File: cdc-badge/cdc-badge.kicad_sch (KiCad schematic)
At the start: 157 parts, among them J1 USB_C, J2 JST S2B-PH-SM4-TB, J3 Conn_02x20_Odd_Even, J4 Conn_Grove, J5 Conn_02x03_Odd_Even, J6 Conn_01x06, J7 Conn_01x24, Q1 Si1308EDL, Q2 Si1308EDL, SW0 0, SW1 1, SW10 YES, SW11 NO, SW12 power on/reset, SW13 reset, SW14 flash/power off, SW15 MST-22D18G2 3J, SW16 MST-22D18G2 3J, SW2 2, SW3 3, SW4 4, SW5 5, SW6 6, SW7 7, SW8 8, SW9 9, U1 ESP32-S3-WROOM-1-N16R8, U2 TCA9535PWR, U3 TR01-C2P-T301, U5 TLV61070ADBVR, U6 BQ25895RTW, U8 TLV62569DBV

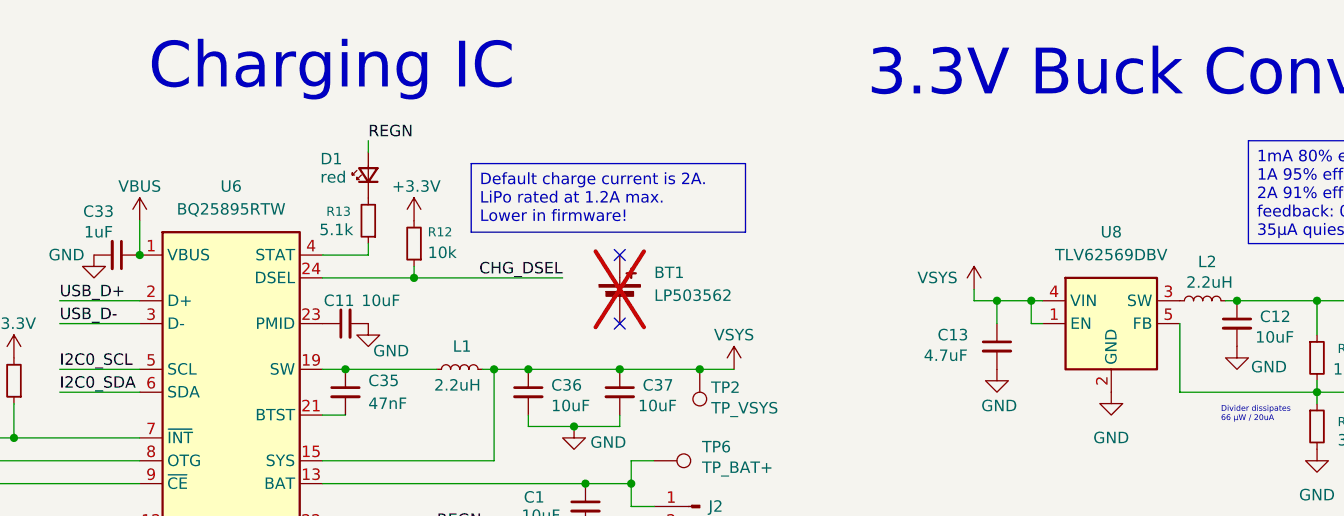
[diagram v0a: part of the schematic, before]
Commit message: Add MPN to all symbols.
Makes BOM ready for other manufacturers besides JLCPCB.
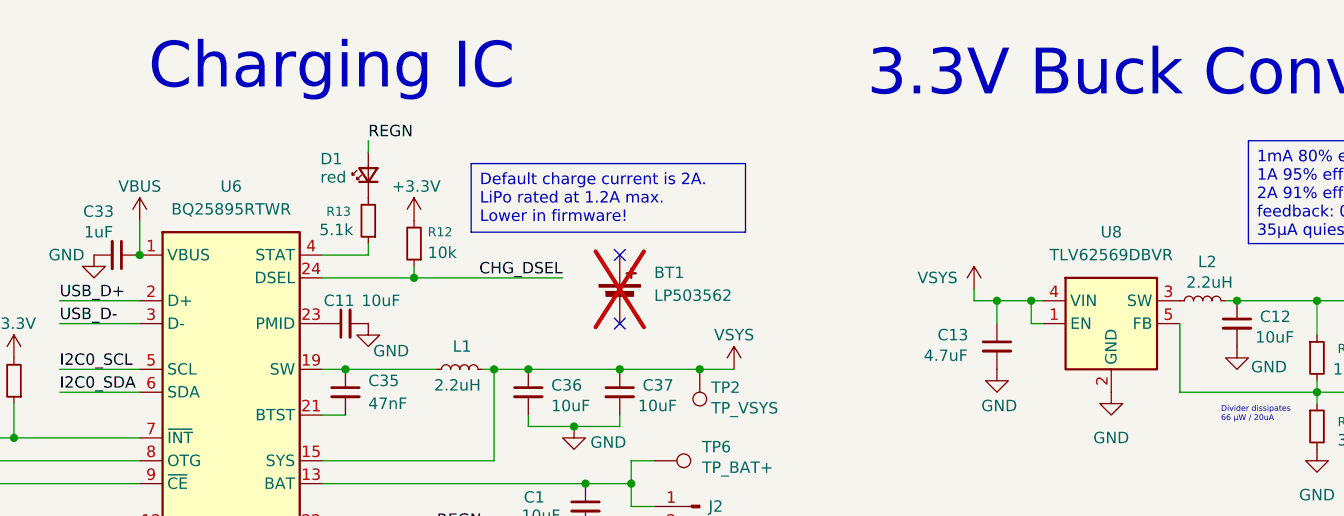
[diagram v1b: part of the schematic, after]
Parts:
- C1, C11, C12, C36, C37, C5, C6, C7, C8, C9: MPN (none) -> CL21A106KAYNNNE
- C10, C15, C16, C17, C18, C19, C2, C20, C21, C22, C25, C26, C27, C28, C29, C3, C30, C31, C32, C4: MPN (none) -> CC0603KRX7R9BB104
- C33: MPN (none) -> CL10A105KB8NNNC
- C35: MPN (none) -> CL10B473KB8NNNC
- D3: MPN (none) -> SMF14CA
- D7, D8: MPN (none) -> H3V3U06B
- J1: MPN (none) -> TYPE-C 16PIN 2MD(073)
- Q1, Q2: MPN (none) -> SI1308EDL
- R10, R16, R18, R23, R24, R25, R26, R27, R28, R29, R3, R30, R31, R36, R37, R38, R39, R40: MPN (none) -> 0603WAF4702T5E
- R12, R14, R15, R20, R4, R42, R43, R46, R47, R5, R6, R8, R9: MPN (none) -> 0603WAF1002T5E
- R32: MPN (none) -> 0603WAF510KT5E
- SW15, SW16: MPN (none) -> MST-22D18G2 3J
- U1: MPN (none) -> ESP32-S3-WROOM-1-N16R8
- U2: MPN (none) -> TCA9535PWR
- U5: MPN (none) -> TLV61070ADBVR
- U6: value BQ25895RTW -> BQ25895RTWR; MPN (none) -> BQ25895RTWR
- U8: value TLV62569DBV -> TLV62569DBVR; MPN (none) -> TLV62569DBVR

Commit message: setup exports, remove unpopulated from BOM
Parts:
- R36, R42, R43, TP1, TP2, TP6, TP7: now left out of the parts list
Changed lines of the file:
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@@
 		(unit 1)
 		(exclude_from_sim no)
-		(in_bom yes)
+		(in_bom no)
 		(on_board yes)
 		(dnp no)
@@
 		(unit 1)
 		(exclude_from_sim no)
-		(in_bom yes)
+		(in_bom no)
 		(on_board yes)
 		(dnp no)
@@
 		(unit 1)
 		(exclude_from_sim no)
-		(in_bom yes)
+		(in_bom no)
 		(on_board yes)
 		(dnp no)
@@
 		(unit 1)
 		(exclude_from_sim no)
-		(in_bom yes)
+		(in_bom no)
 		(on_board yes)
 		(dnp yes)
@@
 		(unit 1)
 		(exclude_from_sim no)
-		(in_bom yes)
+		(in_bom no)
 		(on_board yes)
 		(dnp yes)
@@
 		(unit 1)
 		(exclude_from_sim no)
-		(in_bom yes)
+		(in_bom no)
 		(on_board yes)
 		(dnp yes)
@@
 		(unit 1)
 		(exclude_from_sim no)
-		(in_bom yes)
+		(in_bom no)
 		(on_board yes)
 		(dnp no)

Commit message: Enlarge vias in ESP32 and BQ25895 FPs from 0.2 to 0.3 mm
Makes production cheaper.
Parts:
- U6: footprint Package_DFN_QFN:Texas_RTW_WQFN-24-1EP_4x4mm_P0.5mm_EP2.7x2.7mm_ThermalVias -> CDC_Badge:Texas_RTW_WQFN-24-1EP_4x4mm_P0.5mm_EP2.7x2.7mm_0.3mmThermalVias
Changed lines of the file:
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@@
 			)
 		)
-		(property "Footprint" "Package_DFN_QFN:Texas_RTW_WQFN-24-1EP_4x4mm_P0.5mm_EP2.7x2.7mm_ThermalVias"
+		(property "Footprint" "CDC_Badge:Texas_RTW_WQFN-24-1EP_4x4mm_P0.5mm_EP2.7x2.7mm_0.3mmThermalVias"
 			(at 143.51 92.964 0)
 			(effects

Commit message: Grove connector: new MPN to work with NextPCB
Fix datasheet links in BOOMELE footprints.
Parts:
- J4: MPN HY-4P (A2006WF-04A) -> HC-HY-4AWT
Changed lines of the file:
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@@
 			)
 		)
-		(property "MPN" "HY-4P (A2006WF-04A)"
+		(property "MPN" "HC-HY-4AWT"
 			(at 254 205.74 0)
 			(effects

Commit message: schematic: fix, battery connector was not in BOM
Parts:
- J2: now in the parts list
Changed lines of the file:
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@@
 		(unit 1)
 		(exclude_from_sim no)
-		(in_bom no)
+		(in_bom yes)
 		(on_board yes)
 		(dnp no)

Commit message: pcb: test points, vias, islands
Test points are now SMD again for better aesthetics.
Review via placement.
Fix islands.
Fix silkscreen to via overlap.
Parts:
- TP1, TP2, TP6, TP7: footprint TestPoint:TestPoint_THTPad_D2.0mm_Drill1.0mm -> TestPoint:TestPoint_Pad_D2.0mm
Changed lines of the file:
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@@
 			)
 		)
-		(property "Footprint" "TestPoint:TestPoint_THTPad_D2.0mm_Drill1.0mm"
+		(property "Footprint" "TestPoint:TestPoint_Pad_D2.0mm"
 			(at 190.5 58.42 0)
 			(effects
@@
 			)
 		)
-		(property "Footprint" "TestPoint:TestPoint_THTPad_D2.0mm_Drill1.0mm"
+		(property "Footprint" "TestPoint:TestPoint_Pad_D2.0mm"
 			(at 69.85 44.45 0)
 			(effects
@@
 			)
 		)
-		(property "Footprint" "TestPoint:TestPoint_THTPad_D2.0mm_Drill1.0mm"
+		(property "Footprint" "TestPoint:TestPoint_Pad_D2.0mm"
 			(at 190.5 73.66 0)
 			(effects
@@
 			)
 		)
-		(property "Footprint" "TestPoint:TestPoint_THTPad_D2.0mm_Drill1.0mm"
+		(property "Footprint" "TestPoint:TestPoint_Pad_D2.0mm"
 			(at 193.04 86.36 0)
 			(effects

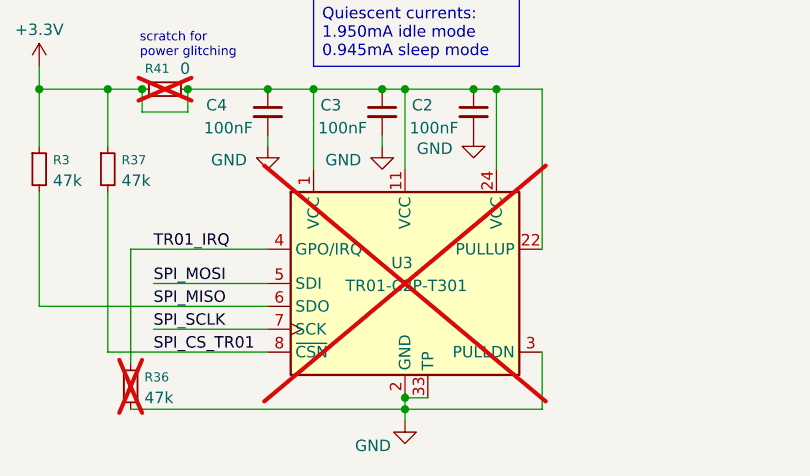
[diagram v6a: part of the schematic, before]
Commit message: schematic: populate TROPIC01
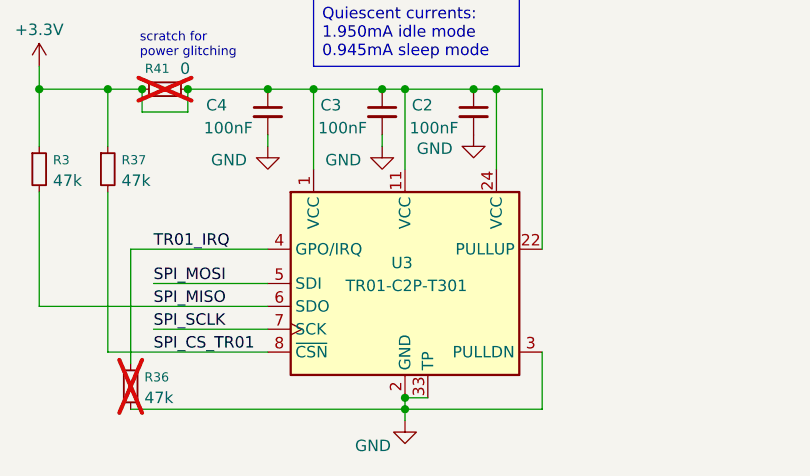
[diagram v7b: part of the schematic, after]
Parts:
- U3: JLCPCB PN (none) -> C9900235223; now fitted; now in the parts list
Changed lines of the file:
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@@
 		(unit 1)
 		(exclude_from_sim no)
-		(in_bom no)
+		(in_bom yes)
 		(on_board yes)
-		(dnp yes)
+		(dnp no)
 		(property "Reference" "U3"
 			(at 275.336 261.874 0)
@@
 			(effects
 				(font
+					(size 1.27 1.27)
+				)
+				(hide yes)
+			)
+		)
+		(property "JLCPCB PN" "C9900235223"
+			(at 276.86 264.16 0)
+			(effects
+				(font

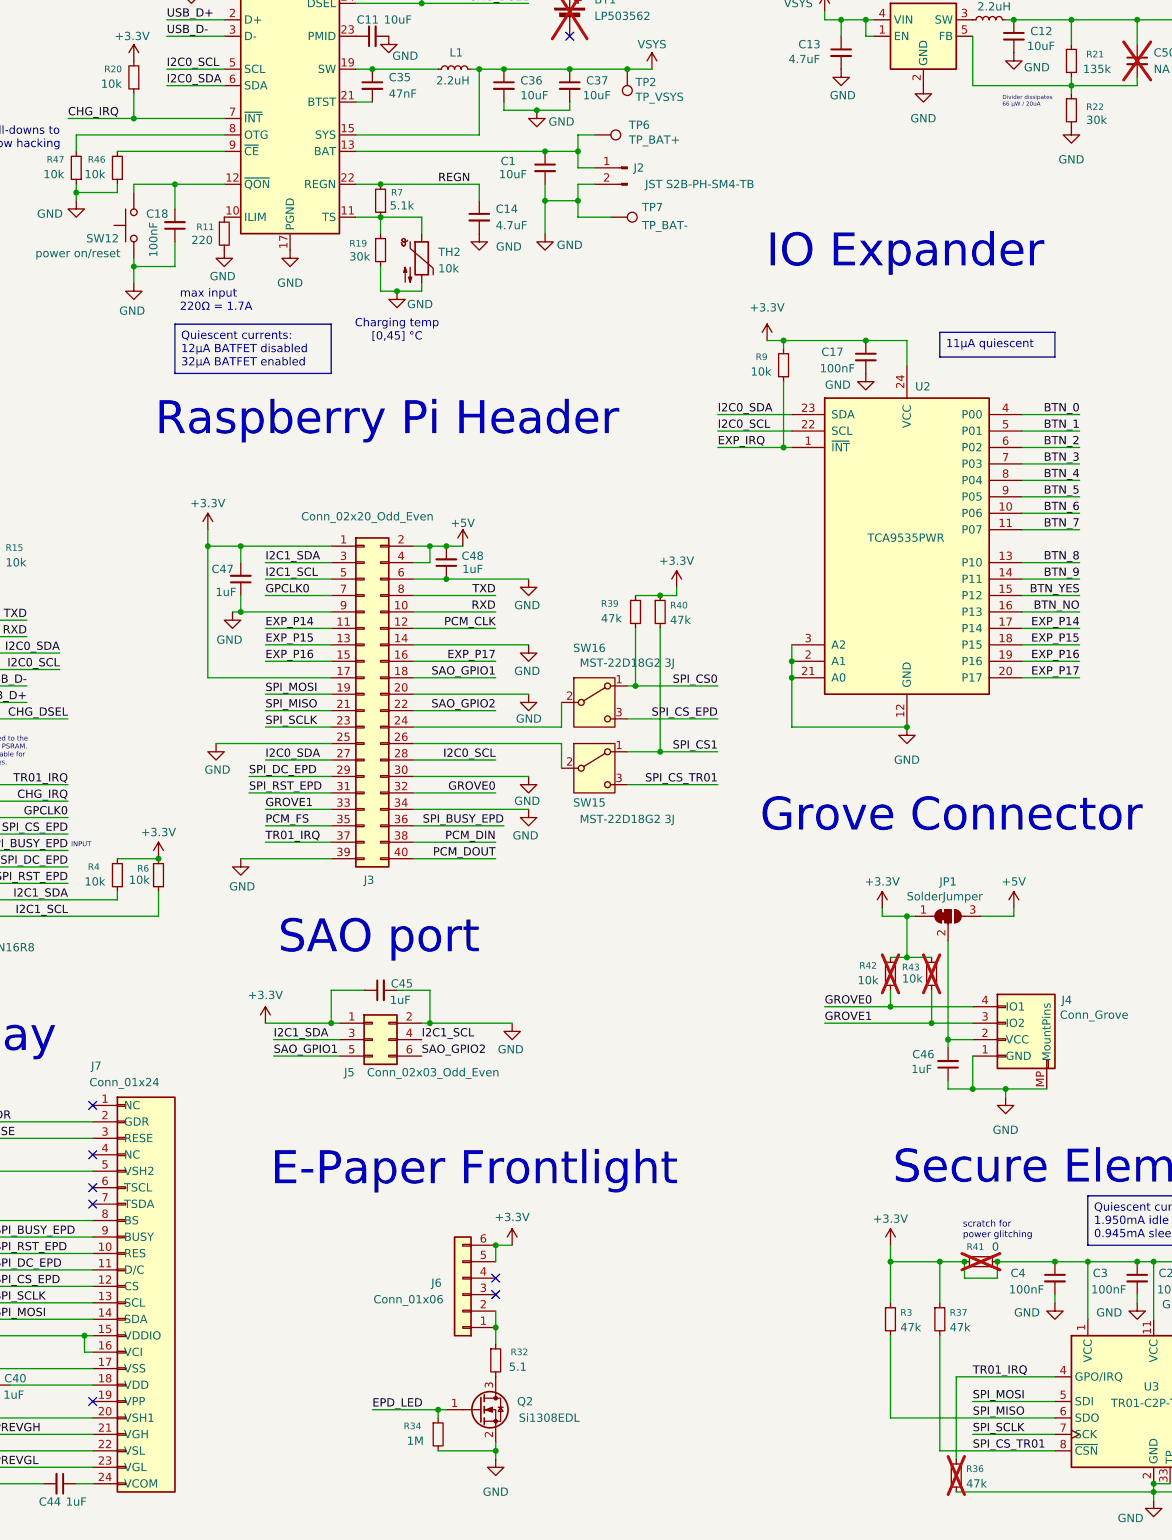
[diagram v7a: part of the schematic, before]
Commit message: schematic: add mounting pins to battery connector
Fixes liking with PCB.
Remove non-generic fields from symbols.
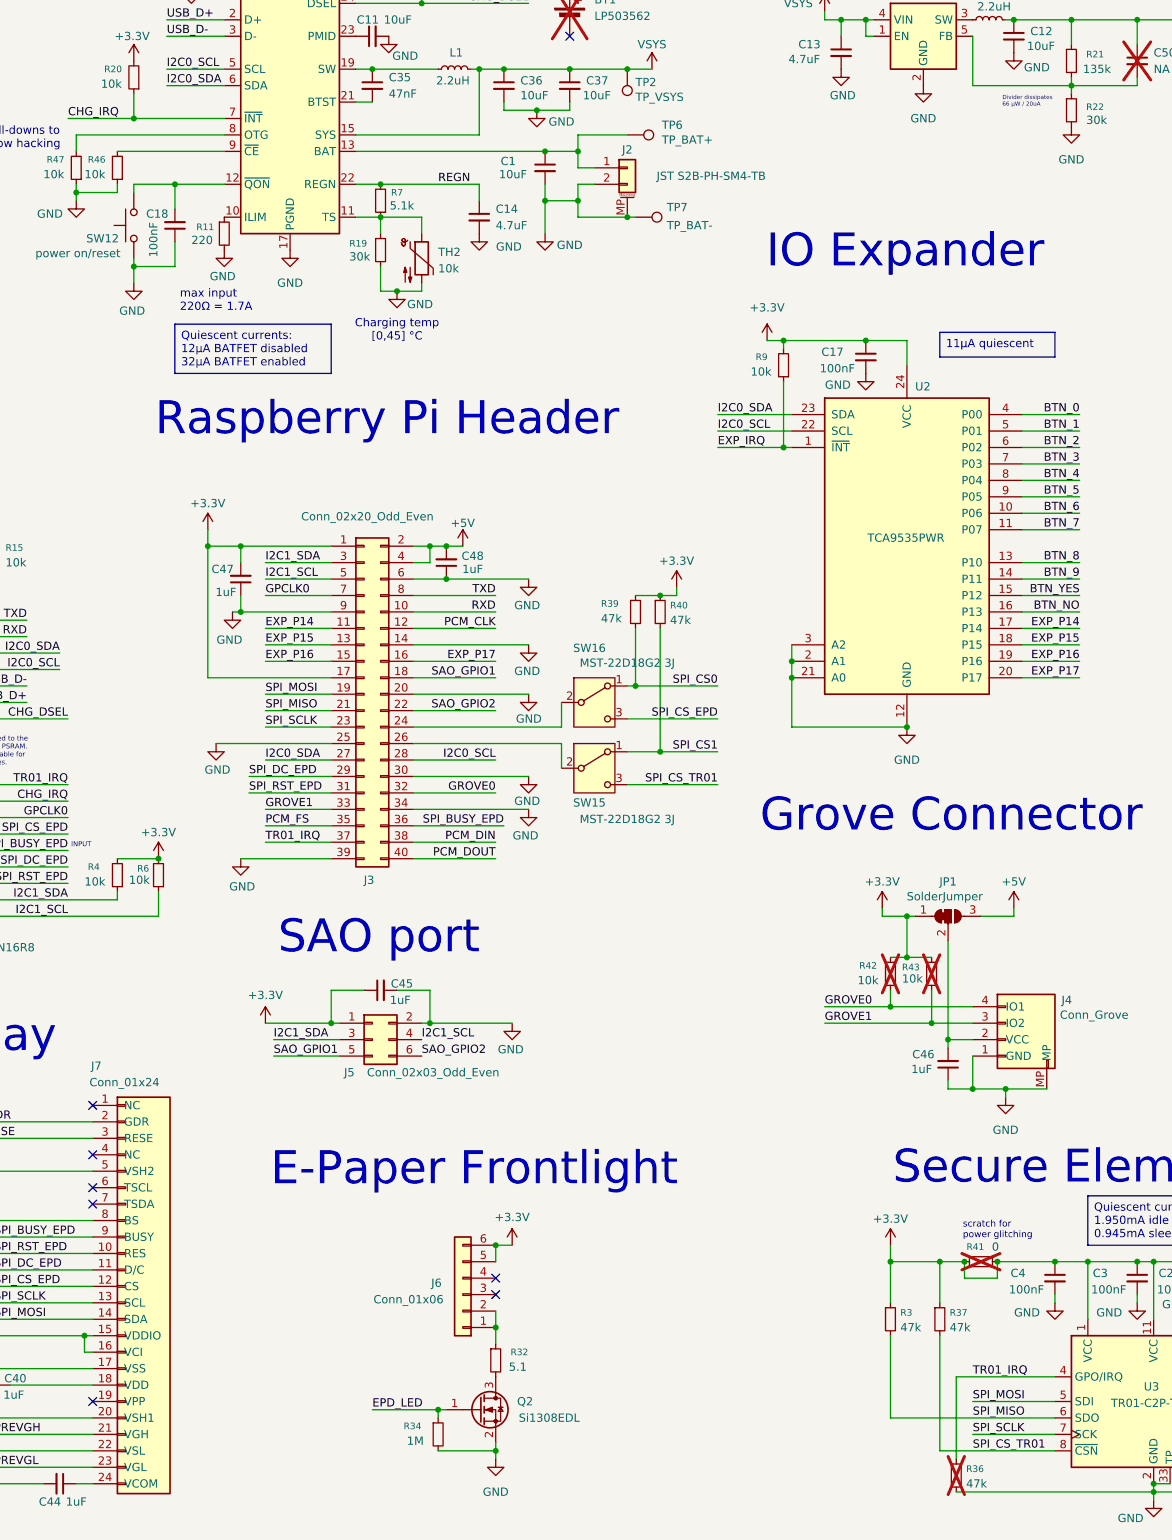
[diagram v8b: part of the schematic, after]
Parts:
- J2: symbol Connector:Conn_01x02_Pin -> Connector_Generic_MountingPin:Conn_01x02_MountingPin
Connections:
- net GND: now also J2.MP (MountPin)
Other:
- moved on the sheet: J4, TP6, TP7
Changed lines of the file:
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@@
 	)
 	(junction
+		(at 195.58 81.28)
+		(diameter 0)
+		(color 0 0 0 0)
+	)
+	(junction
 		(at 243.84 242.57)
 		(diameter 0)
@@
 	(wire
 		(pts
+			(xy 196.85 81.28) (xy 195.58 81.28)
+		)
+		(stroke
+			(width 0)
+			(type default)
+		)
+	)
+	(wire
+		(pts
 			(xy 92.71 229.87) (xy 92.71 228.6)
 		)
@@
 	(wire
 		(pts
-			(xy 193.04 81.28) (xy 187.96 81.28)
+			(xy 195.58 81.28) (xy 187.96 81.28)
 		)
 		(stroke
@@
 	(wire
 		(pts
-			(xy 190.5 68.58) (xy 187.96 68.58)
+			(xy 195.58 68.58) (xy 187.96 68.58)
 		)
 		(stroke
@@
 	(symbol
 		(lib_id "Connector:TestPoint")
-		(at 190.5 68.58 270)
+		(at 195.58 68.58 270)
 		(unit 1)
 		(exclude_from_sim no)
@@
 		(dnp no)
 		(property "Reference" "TP6"
-			(at 195.834 67.056 90)
+			(at 200.914 67.056 90)
 			(effects
 				(font
@@
 		)
 		(property "Value" "TP_BAT+"
-			(at 195.834 69.342 90)
+			(at 200.914 69.342 90)
 			(effects
 				(font
@@
 		)
 		(property "Footprint" "TestPoint:TestPoint_Pad_D2.0mm"
-			(at 190.5 73.66 0)
+			(at 195.58 73.66 0)
 			(effects
 				(font
@@
 		)
 		(property "Datasheet" "~"
-			(at 190.5 73.66 0)
+			(at 195.58 73.66 0)
 			(effects
 				(font
@@
 		)
 		(property "Description" "test point"
-			(at 190.5 68.58 0)
+			(at 195.58 68.58 0)
 			(effects
 				(font
@@
 	(symbol
 		(lib_id "Connector:TestPoint")
-		(at 193.04 81.28 270)
+		(at 196.85 81.28 270)
 		(unit 1)
 		(exclude_from_sim no)
@@
 		(dnp no)
 		(property "Reference" "TP7"
-			(at 197.866 79.756 90)
+			(at 201.676 79.756 90)
 			(effects
 				(font
@@
 		)
 		(property "Value" "TP_BAT-"
-			(at 197.866 82.55 90)
+			(at 201.676 82.55 90)
 			(effects
 				(font
@@
 		)
 		(property "Footprint" "TestPoint:TestPoint_Pad_D2.0mm"
-			(at 193.04 86.36 0)
+			(at 196.85 86.36 0)
 			(effects
 				(font
@@
 		)
 		(property "Datasheet" "~"
-			(at 193.04 86.36 0)
+			(at 196.85 86.36 0)
 			(effects
 				(font
@@
 		)
 		(property "Description" "test point"
-			(at 193.04 81.28 0)
+			(at 196.85 81.28 0)
 			(effects
 				(font
@@
 	)
 	(symbol
-		(lib_id "Connector:Conn_01x02_Pin")
+		(lib_id "Connector_Generic_MountingPin:Conn_01x02_MountingPin")
 		(at 195.58 73.66 0)
-		(mirror y)
 		(unit 1)
 		(exclude_from_sim no)
@@
 		(dnp no)
 		(property "Reference" "J2"
-			(at 197.358 73.66 0)
+			(at 195.58 70.866 0)
 			(effects
 				(font
@@
 		)
 		(property "Value" "JST S2B-PH-SM4-TB"
-			(at 206.756 76.2 0)
+			(at 208.534 74.93 0)
 			(effects
 				(font
@@
 		(pin "1"
 		)
+		(pin "MP"
+		)
 		(instances
